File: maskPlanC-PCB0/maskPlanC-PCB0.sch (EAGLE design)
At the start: 9 parts, among them U1 ATTINY85-20PU

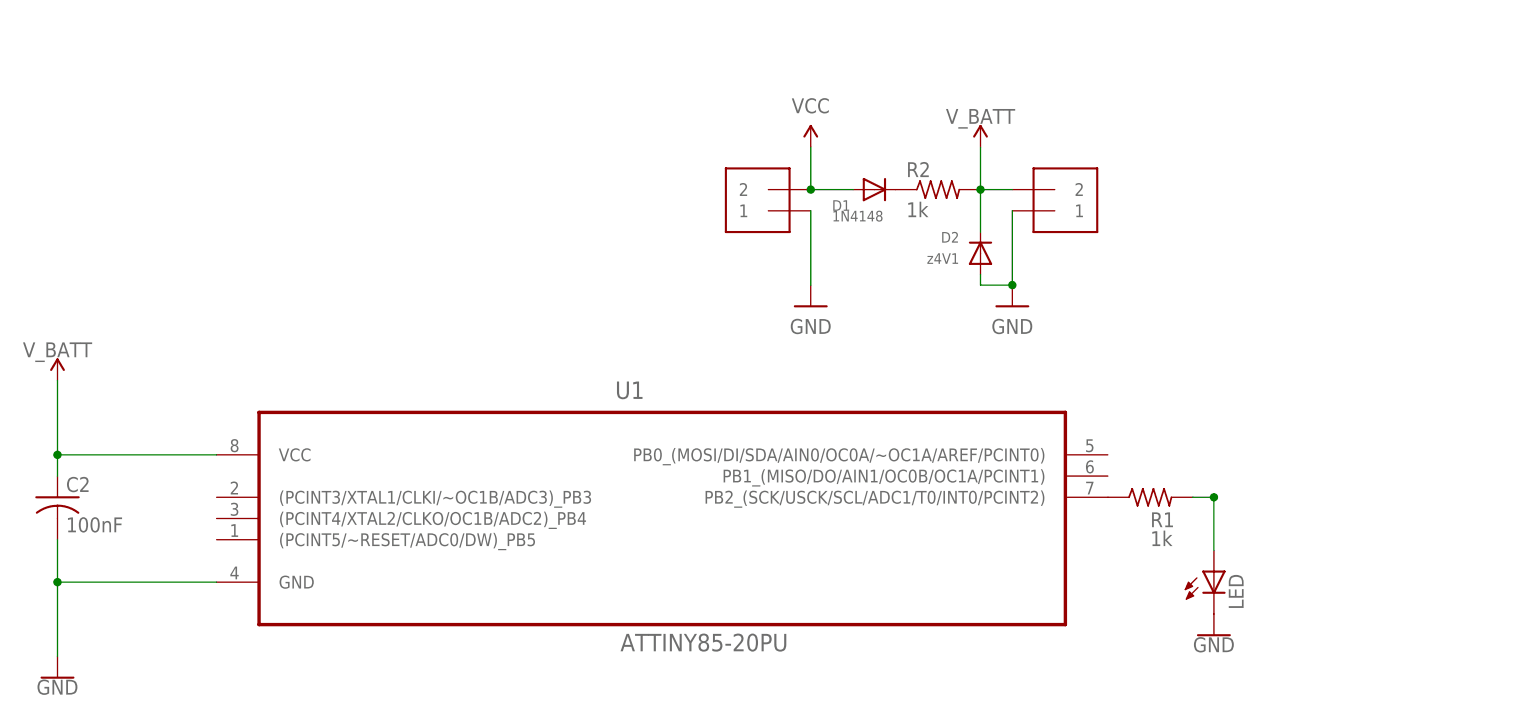
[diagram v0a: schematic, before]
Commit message: added PCB & software for matrix2
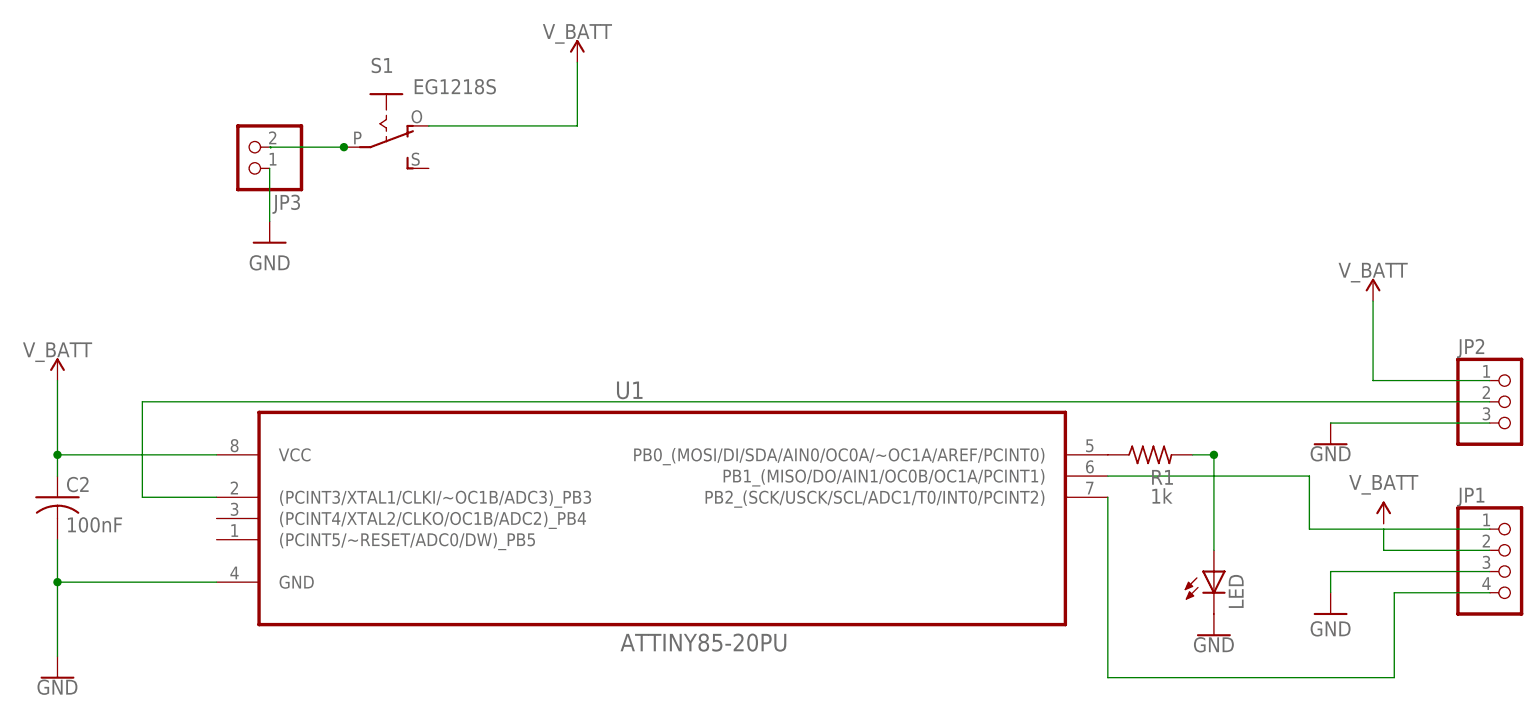
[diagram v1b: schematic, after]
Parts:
- removed BAT, CHG: 1X2-3.5MM, adafruit:1X2-3.5MM
- removed D1: 1N4148, adafruit:DIODEDO-1N4148
- removed D2: z4V1, adafruit:DIODEDO-1N4148
- removed R2: 1k, adafruit:R-US_0204/7
- added JP1: (no value), pinhead:PINHD-1X4
- added JP2: (no value), pinhead:PINHD-1X3
- added JP3: (no value), pinhead:PINHD-1X2
- added S1: EG1218S, EG1218:EG1218S
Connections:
- removed net VCC: CHG.2, D1.A
- new net N$3: JP3.2, S1.P
- new net N$4: JP1.2
- new net N$5: JP2.2, U1.(PCINT3/XTAL1/CLKI/~OC1B/ADC3)_PB3
- new net N$7: JP1.4, U1.PB2_(SCK/USCK/SCL/ADC1/T0/INT0/PCINT2)
- net GND: now also JP1.3, JP2.3, JP3.1; no longer BAT.1, CHG.1, D2.A
- net N$1: now also JP1.1, U1.PB1_(MISO/DO/AIN1/OC0B/OC1A/PCINT1); no longer R1.1, U1.PB2_(SCK/USCK/SCL/ADC1/T0/INT0/PCINT2)
- net N$6: now also R1.1, U1.PB0_(MOSI/DI/SDA/AIN0/OC0A/~OC1A/AREF/PCINT0); no longer D1.C, R2.1
- net V_BATT: now also JP2.1, S1.O; no longer BAT.2, D2.C, R2.2
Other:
- moved on the sheet: R1

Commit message: PCB routed
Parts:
- renumbered JP1 to SENS, JP2 to PIX, JP3 to BAT
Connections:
- removed net N$4: SENS.2
- net V_BATT: now also SENS.2
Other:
- moved on the sheet: R1
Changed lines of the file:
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@@
 <setting verticaltext="up"/>
 </settings>
-<grid distance="50" unitdist="mil" unit="mil" style="lines" multiple="1" display="no" altdistance="0.01" altunitdist="inch" altunit="inch"/>
+<grid distance="0.1" unitdist="inch" unit="inch" style="lines" multiple="1" display="no" altdistance="0.01" altunitdist="inch" altunit="inch"/>
 <layers>
 <layer number="1" name="Top" color="4" fill="1" visible="no" active="no"/>
@@
 <part name="SUPPLY3" library="SparkFun-PowerSymbols" library_urn="urn:adsk.eagle:library:530" deviceset="V_BATT" device=""/>
 <part name="S1" library="EG1218" deviceset="EG1218" device="S"/>
-<part name="JP1" library="pinhead" library_urn="urn:adsk.eagle:library:325" deviceset="PINHD-1X4" device="" package3d_urn="urn:adsk.eagle:package:22407/2"/>
-<part name="JP2" library="pinhead" library_urn="urn:adsk.eagle:library:325" deviceset="PINHD-1X3" device="" package3d_urn="urn:adsk.eagle:package:22458/2"/>
+<part name="SENS" library="pinhead" library_urn="urn:adsk.eagle:library:325" deviceset="PINHD-1X4" device="" package3d_urn="urn:adsk.eagle:package:22407/2"/>
+<part name="PIX" library="pinhead" library_urn="urn:adsk.eagle:library:325" deviceset="PINHD-1X3" device="" package3d_urn="urn:adsk.eagle:package:22458/2"/>
 <part name="GND2" library="SparkFun-PowerSymbols" library_urn="urn:adsk.eagle:library:530" deviceset="GND" device=""/>
 <part name="GND5" library="SparkFun-PowerSymbols" library_urn="urn:adsk.eagle:library:530" deviceset="GND" device=""/>
 <part name="SUPPLY2" library="SparkFun-PowerSymbols" library_urn="urn:adsk.eagle:library:530" deviceset="V_BATT" device=""/>
 <part name="SUPPLY4" library="SparkFun-PowerSymbols" library_urn="urn:adsk.eagle:library:530" deviceset="V_BATT" device=""/>
-<part name="JP3" library="pinhead" library_urn="urn:adsk.eagle:library:325" deviceset="PINHD-1X2" device="" package3d_urn="urn:adsk.eagle:package:22435/2"/>
+<part name="BAT" library="pinhead" library_urn="urn:adsk.eagle:library:325" deviceset="PINHD-1X2" device="" package3d_urn="urn:adsk.eagle:package:22435/2"/>
 </parts>
 <sheets>
@@
 <attribute name="VALUE" x="11.43" y="55.626" size="1.778" layer="96" align="top-center"/>
 </instance>
-<instance part="R1" gate="G$1" x="142.24" y="82.55" smashed="yes">
-<attribute name="NAME" x="142.24" y="78.9686" size="1.778" layer="95"/>
-<attribute name="VALUE" x="142.24" y="76.708" size="1.778" layer="96"/>
+<instance part="R1" gate="G$1" x="144.78" y="82.55" smashed="yes">
+<attribute name="NAME" x="144.78" y="78.9686" size="1.778" layer="95"/>
+<attribute name="VALUE" x="144.78" y="76.708" size="1.778" layer="96"/>
 </instance>
 <instance part="C2" gate="G$1" x="11.43" y="77.47" smashed="yes">
@@
 <attribute name="VALUE" x="12.446" y="73.279" size="1.778" layer="96"/>
 </instance>
-<instance part="GND4" gate="1" x="36.83" y="107.95" smashed="yes">
-<attribute name="VALUE" x="36.83" y="106.426" size="1.778" layer="96" align="top-center"/>
+<instance part="GND4" gate="1" x="45.72" y="114.3" smashed="yes">
+<attribute name="VALUE" x="45.72" y="112.776" size="1.778" layer="96" align="top-center"/>
 </instance>
 <instance part="SUPPLY1" gate="G$1" x="73.66" y="129.54" smashed="yes">
@@
 <instance part="S1" gate="1" x="50.8" y="121.92" smashed="yes" rot="R270">
 <attribute name="NAME" x="48.895" y="128.27" size="1.778" layer="95"/>
-<attribute name="VALUE" x="53.975" y="125.73" size="1.778" layer="96"/>
-</instance>
-<instance part="JP1" gate="A" x="185.42" y="68.58" smashed="yes">
+<attribute name="VALUE" x="53.975" y="113.03" size="1.778" layer="96"/>
+</instance>
+<instance part="SENS" gate="A" x="185.42" y="68.58" smashed="yes">
 <attribute name="NAME" x="179.07" y="76.835" size="1.778" layer="95"/>
 <attribute name="VALUE" x="179.07" y="60.96" size="1.778" layer="96"/>
 </instance>
-<instance part="JP2" gate="A" x="185.42" y="88.9" smashed="yes">
+<instance part="PIX" gate="A" x="185.42" y="88.9" smashed="yes">
 <attribute name="NAME" x="179.07" y="94.615" size="1.778" layer="95"/>
 <attribute name="VALUE" x="179.07" y="81.28" size="1.778" layer="96"/>
 </instance>
-<instance part="GND2" gate="1" x="163.83" y="83.82" smashed="yes">
-<attribute name="VALUE" x="163.83" y="83.566" size="1.778" layer="96" align="top-center"/>
-</instance>
-<instance part="GND5" gate="1" x="163.83" y="63.5" smashed="yes">
-<attribute name="VALUE" x="163.83" y="62.611" size="1.778" layer="96" align="top-center"/>
+<instance part="GND2" gate="1" x="168.91" y="83.82" smashed="yes">
+<attribute name="VALUE" x="168.91" y="83.566" size="1.778" layer="96" align="top-center"/>
+</instance>
+<instance part="GND5" gate="1" x="162.56" y="63.5" smashed="yes">
+<attribute name="VALUE" x="162.56" y="62.611" size="1.778" layer="96" align="top-center"/>
 </instance>
 <instance part="SUPPLY2" gate="G$1" x="168.91" y="100.965" smashed="yes">
 <attribute name="VALUE" x="168.91" y="103.759" size="1.778" layer="96" align="bottom-center"/>
 </instance>
-<instance part="SUPPLY4" gate="G$1" x="170.18" y="74.295" smashed="yes">
-<attribute name="VALUE" x="170.18" y="78.359" size="1.778" layer="96" align="bottom-center"/>
-</instance>
-<instance part="JP3" gate="G$1" x="34.29" y="119.38" smashed="yes" rot="R180">
-<attribute name="NAME" x="40.64" y="113.665" size="1.778" layer="95" rot="R180"/>
+<instance part="SUPPLY4" gate="G$1" x="162.56" y="73.533" smashed="yes">
+<attribute name="VALUE" x="162.56" y="77.597" size="1.778" layer="96" align="bottom-center"/>
+</instance>
+<instance part="BAT" gate="G$1" x="34.29" y="119.38" smashed="yes" rot="R180">
+<attribute name="NAME" x="38.1" y="124.46" size="1.778" layer="95" rot="R180"/>
 <attribute name="VALUE" x="40.64" y="124.46" size="1.778" layer="96" rot="R180"/>
 </instance>
@@
 <segment>
 <pinref part="GND4" gate="1" pin="GND"/>
-<wire x1="36.83" y1="110.49" x2="36.83" y2="116.84" width="0.1524" layer="91"/>
-<pinref part="JP3" gate="G$1" pin="1"/>
-</segment>
-<segment>
-<pinref part="JP2" gate="A" pin="3"/>
-<wire x1="163.83" y1="86.36" x2="182.88" y2="86.36" width="0.1524" layer="91"/>
+<wire x1="45.72" y1="116.84" x2="36.83" y2="116.84" width="0.1524" layer="91"/>
+<pinref part="BAT" gate="G$1" pin="1"/>
+</segment>
+<segment>
+<pinref part="PIX" gate="A" pin="3"/>
+<wire x1="168.91" y1="86.36" x2="182.88" y2="86.36" width="0.1524" layer="91"/>
 <pinref part="GND2" gate="1" pin="GND"/>
 </segment>
 <segment>
-<pinref part="JP1" gate="A" pin="3"/>
+<pinref part="SENS" gate="A" pin="3"/>
 <pinref part="GND5" gate="1" pin="GND"/>
-<wire x1="182.88" y1="68.58" x2="163.83" y2="68.58" width="0.1524" layer="91"/>
-<wire x1="163.83" y1="68.58" x2="163.83" y2="66.04" width="0.1524" layer="91"/>
+<wire x1="182.88" y1="68.58" x2="162.56" y2="68.58" width="0.1524" layer="91"/>
+<wire x1="162.56" y1="68.58" x2="162.56" y2="66.04" width="0.1524" layer="91"/>
 </segment>
 </net>
@@
 <pinref part="LED" gate="G$1" pin="A"/>
 <wire x1="149.86" y1="71.12" x2="149.86" y2="82.55" width="0.1524" layer="91"/>
-<wire x1="149.86" y1="82.55" x2="147.32" y2="82.55" width="0.1524" layer="91"/>
 <junction x="149.86" y="82.55"/>
 </segment>
@@
 <wire x1="168.91" y1="100.965" x2="168.91" y2="91.44" width="0.1524" layer="91"/>
 <pinref part="SUPPLY2" gate="G$1" pin="V_BATT"/>
-<pinref part="JP2" gate="A" pin="1"/>
+<pinref part="PIX" gate="A" pin="1"/>
 <wire x1="182.88" y1="91.44" x2="168.91" y2="91.44" width="0.1524" layer="91"/>
+</segment>
+<segment>
+<pinref part="SENS" gate="A" pin="2"/>
+<wire x1="162.56" y1="71.12" x2="182.88" y2="71.12" width="0.1524" layer="91"/>
+<wire x1="162.56" y1="73.66" x2="162.56" y2="73.533" width="0.1524" layer="91"/>
+<pinref part="SUPPLY4" gate="G$1" pin="V_BATT"/>
+<wire x1="162.56" y1="73.533" x2="162.56" y2="71.12" width="0.1524" layer="91"/>
+<junction x="162.56" y="73.533"/>
 </segment>
 </net>
@@
 <pinref part="S1" gate="1" pin="P"/>
 <junction x="45.72" y="119.38"/>
-<pinref part="JP3" gate="G$1" pin="2"/>
-</segment>
-</net>
-<net name="N$4" class="0">
-<segment>
-<pinref part="JP1" gate="A" pin="2"/>
-<wire x1="170.18" y1="73.66" x2="170.18" y2="71.12" width="0.1524" layer="91"/>
-<wire x1="170.18" y1="71.12" x2="182.88" y2="71.12" width="0.1524" layer="91"/>
+<pinref part="BAT" gate="G$1" pin="2"/>
 </segment>
 </net>
 <net name="N$5" class="0">
 <segment>
-<pinref part="JP2" gate="A" pin="2"/>
+<pinref part="PIX" gate="A" pin="2"/>
 <wire x1="182.88" y1="88.9" x2="21.59" y2="88.9" width="0.1524" layer="91"/>
 <wire x1="21.59" y1="88.9" x2="21.59" y2="77.47" width="0.1524" layer="91"/>
@@
 <pinref part="R1" gate="G$1" pin="1"/>
 <pinref part="U1" gate="A" pin="PB0_(MOSI/DI/SDA/AIN0/OC0A/~OC1A/AREF/PCINT0)"/>
+<wire x1="139.7" y1="82.55" x2="137.16" y2="82.55" width="0.1524" layer="91"/>
 </segment>
 </net>
@@
 <segment>
 <pinref part="U1" gate="A" pin="PB1_(MISO/DO/AIN1/OC0B/OC1A/PCINT1)"/>
-<wire x1="137.16" y1="80.01" x2="161.29" y2="80.01" width="0.1524" layer="91"/>
-<wire x1="161.29" y1="80.01" x2="161.29" y2="73.66" width="0.1524" layer="91"/>
-<pinref part="JP1" gate="A" pin="1"/>
-<wire x1="161.29" y1="73.66" x2="182.88" y2="73.66" width="0.1524" layer="91"/>
+<wire x1="137.16" y1="80.01" x2="173.99" y2="80.01" width="0.1524" layer="91"/>
+<wire x1="173.99" y1="80.01" x2="173.99" y2="73.66" width="0.1524" layer="91"/>
+<pinref part="SENS" gate="A" pin="1"/>
+<wire x1="173.99" y1="73.66" x2="182.88" y2="73.66" width="0.1524" layer="91"/>
 </segment>
 </net>
 <net name="N$7" class="0">
 <segment>
-<pinref part="JP1" gate="A" pin="4"/>
+<pinref part="SENS" gate="A" pin="4"/>
 <wire x1="182.88" y1="66.04" x2="171.45" y2="66.04" width="0.1524" layer="91"/>
 <wire x1="171.45" y1="66.04" x2="171.45" y2="55.88" width="0.1524" layer="91"/>
